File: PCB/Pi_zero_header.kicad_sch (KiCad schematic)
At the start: 44 parts, among them J1 Raspberry_Pi_2_3, J2 USB_C_Receptacle_USB2.0, U1 RP2040, U2 W25Q128JVS, U3 TB6612FNG, U6 PQ25792RQMR, Y1 Crystal

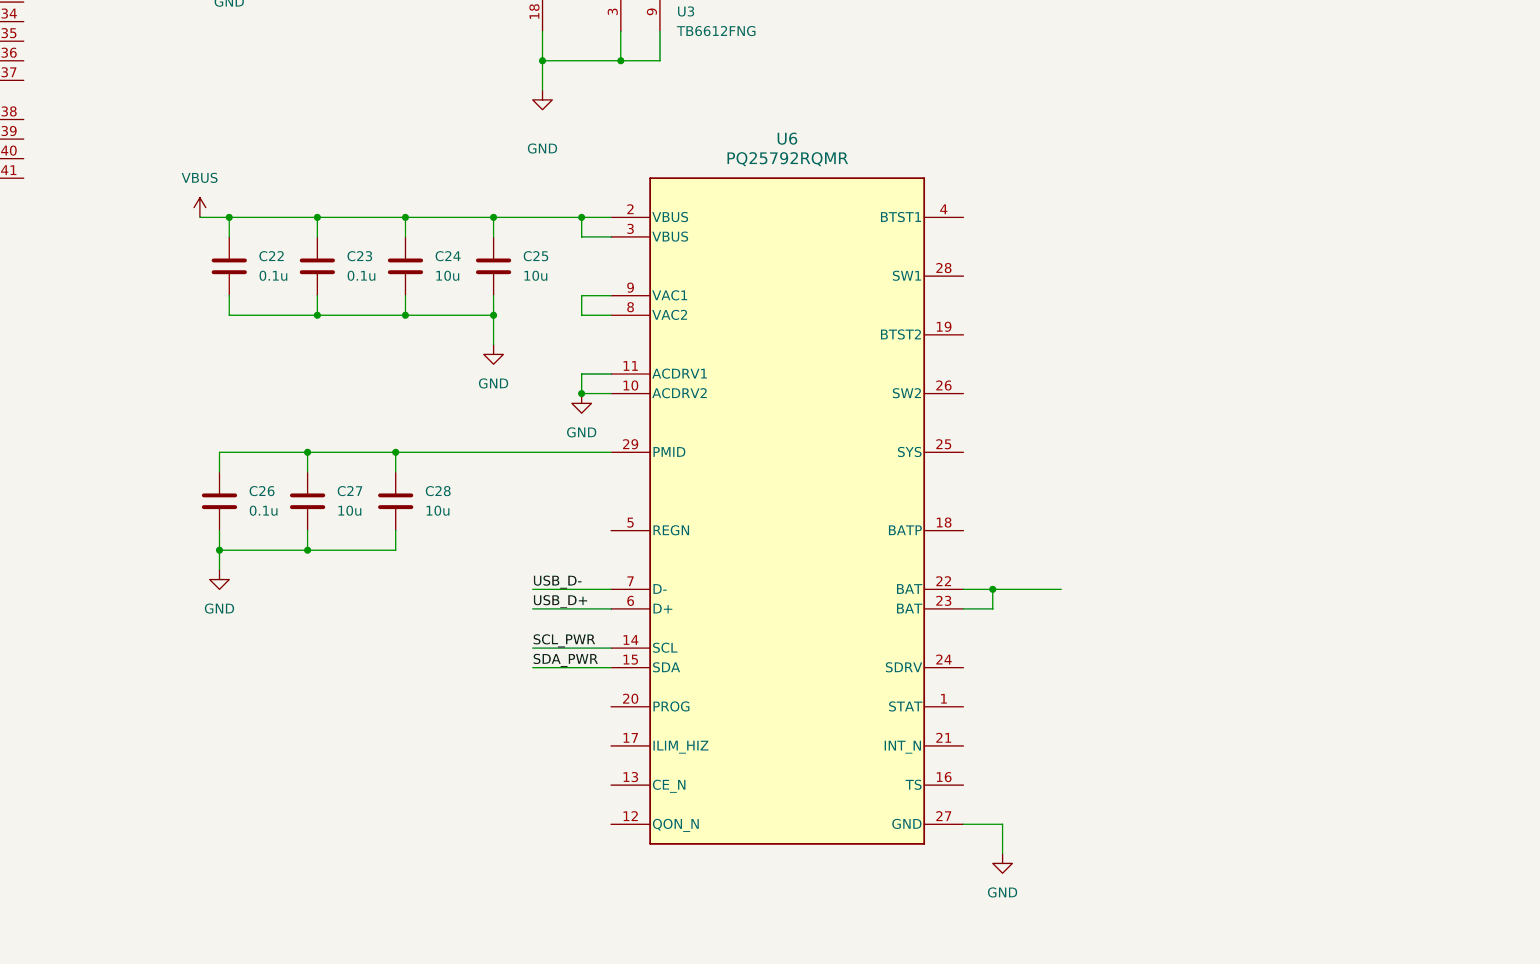
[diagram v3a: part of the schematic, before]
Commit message: Edited schema
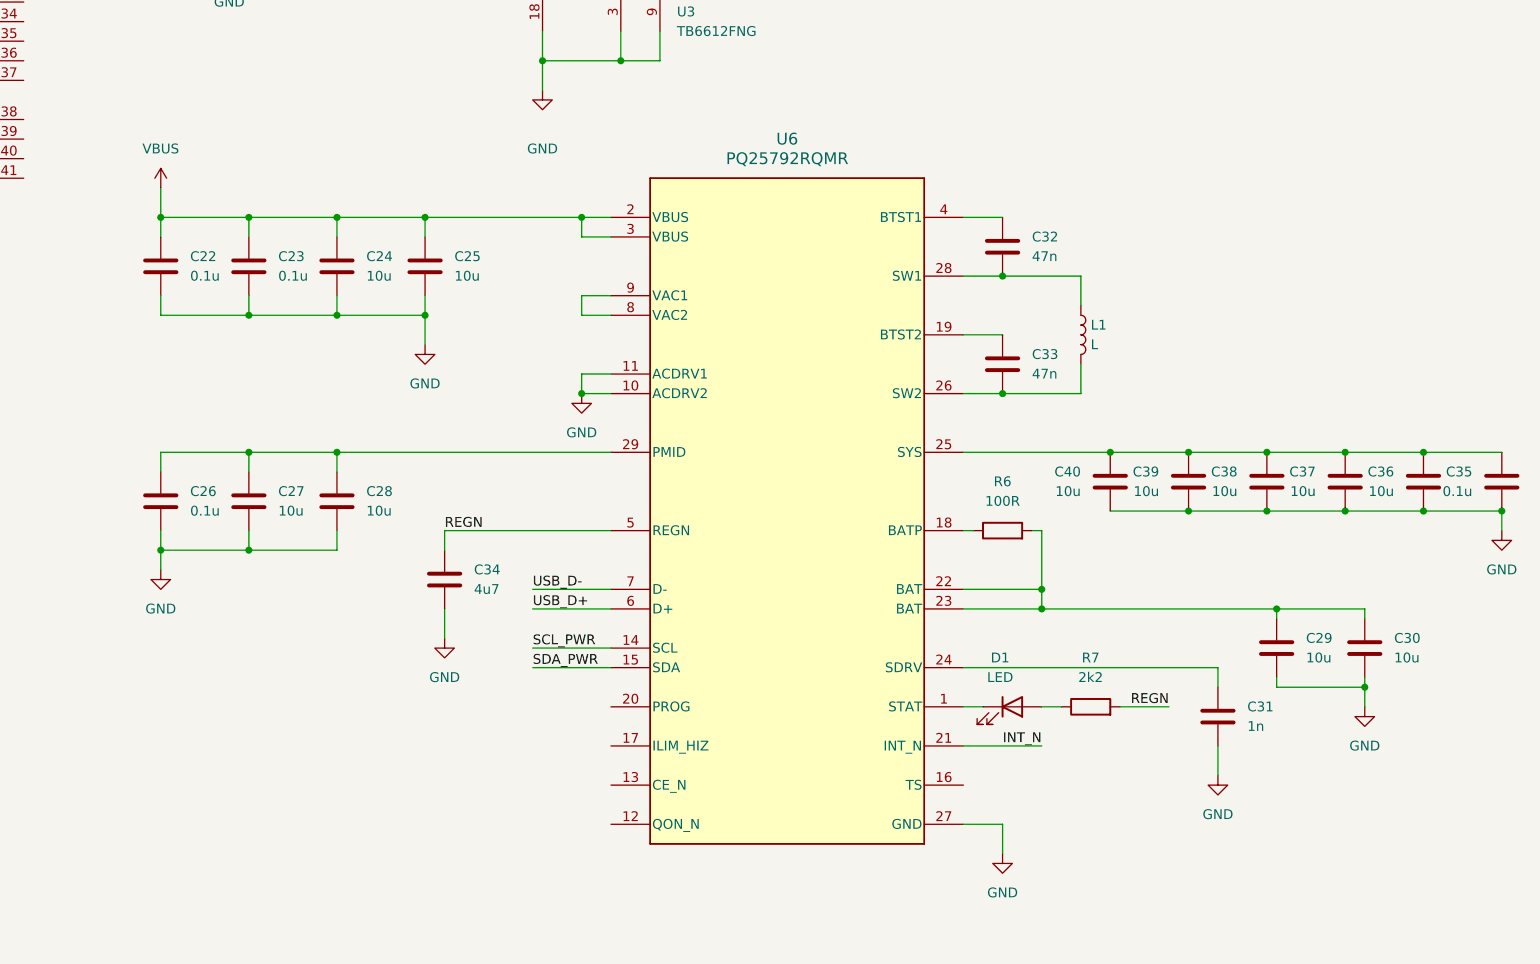
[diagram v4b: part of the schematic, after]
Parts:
- added C29, C30, C36, C37, C38, C39, C40: 10u, symbol Device:C
- added C31: 1n, symbol Device:C
- added C32, C33: 47n, symbol Device:C
- added C34: 4u7, symbol Device:C
- added C35: 0.1u, symbol Device:C
- added D1: LED, symbol Device:LED
- added L1: L, symbol Device:L
- added R6: 100R, symbol Device:R
- added R7: 2k2, symbol Device:R
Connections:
- net GND: now also C29.2, C30.2, C31.2, C34.2, C35.2, C36.2, C37.2, C38.2, C39.2, C40.2
- net at U6.1 (STAT): now also D1.1 (K)
- net at U6.18 (BATP): now also R6.1
- net at U6.19 (BTST2): now also C33.1
- net INT_N: now reaches U6.21 (INT_N)
- net at U6.22 (BAT), U6.23 (BAT): now also C29.1, C30.1, R6.2
- net at U6.24 (SDRV): now also C31.1
- net at U6.25 (SYS): now also C35.1, C36.1, C37.1, C38.1, C39.1, C40.1
- net at U6.26 (SW2): now also C33.2, L1.2
- net at U6.28 (SW1): now also C32.2, L1.1
- net at U6.4 (BTST1): now also C32.1
- net REGN: now reaches U6.5 (REGN)
- net REGN: now also C34.1, R7.2
- new net: D1.2 (A), R7.1
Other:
- moved on the sheet: C22, C23, C24, C25, C26, C27, C28

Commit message: Some changes
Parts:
- removed C1, C4: 10u, symbol Device:C
- added J3, J4: Screw_Terminal_01x02, TerminalBlock_TE-Connectivity:TerminalBlock_TE_282834-2_1x02_P2.54mm_Horizontal, symbol Connector:Screw_Terminal_01x02
- added SW1: SW_Push, Button_Switch_SMD:SW_Push_1P1T_NO_Vertical_Wuerth_434133025816, symbol Switch:SW_Push
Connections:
- net +5V: no longer C18.1, C19.1, U3.13 (VM2), U3.14 (VM3), U3.24 (VM1)
- net GND: now also SW1.1
- net VDD: now reaches C35.1, C36.1, C37.1, C38.1, C39.1, C40.1, U6.25 (SYS)
- net VDD: now also C18.1, C19.1, U3.13 (VM2), U3.14 (VM3), U3.24 (VM1)
- net at R1.1: now also SW1.2
- net at U3.1 (AO1), U3.2 (AO1): now also J3.1 (Pin_1)
- net at U3.11 (BO1), U3.12 (BO1): now also J4.1 (Pin_1)
- net at U3.5 (AO2), U3.6 (AO2): now also J3.2 (Pin_2)
- net at U3.7 (BO2), U3.8 (BO2): now also J4.2 (Pin_2)
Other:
- moved on the sheet: C10, C11, C12, C13, C14, C15, C16, C17, C18, C19, C2, C20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

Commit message: Bruuuh...
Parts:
- added R10: 10k, symbol Device:R
- added R11: 6k04, symbol Device:R
- added R12: 127k, symbol Device:R
- added R13: 100k, symbol Device:R
- added R8: 5k24, symbol Device:R
- added R9: 30k31, symbol Device:R
- C18, C20, C22, C23, C26, C35: value 0.1u -> 100n
- L1: value L -> 1u
- R7: value 2k2 -> 3k3
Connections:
- net GND: now also R10.2, R11.2, R13.2, R9.2
- net REGN: now also R12.2, R8.2
- net USB_D+: no longer U6.6 (D+)
- net USB_D-: no longer U6.7 (D-)
- net at U6.16 (TS): now also R10.1, R8.1, R9.1
- net at U6.17 (ILIM_HIZ): now also R12.1, R13.1
- net at U6.20 (PROG): now also R11.1
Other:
- moved on the sheet: C29, C30, C31, C34, R7

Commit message: Added buck-boost converter to schema
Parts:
- added C1, C4, C41, C43: 10u, symbol Device:C
- added C42: 100n, symbol Device:C
- added C44, C45, C46: 22u, symbol Device:C
- added L2: 1u, symbol Device:L
- added R14: 10k, symbol Device:R
- added R15: 680k, symbol Device:R
- added R16: 100k, symbol Device:R
- added R17: 130k, symbol Device:R
- added U4: TPS630701RNMR, RNM0015A:RNM0015A, symbol TPS63070RNMR:TPS630701RNMR
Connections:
- net +5V: now also C43.1, C44.1, C45.1, C46.1, R15.1, R16.1, U4.7 (VOUT), U4.8 (VOUT)
- net GND: now also C1.2, C4.2, C41.2, C42.2, C43.2, C44.2, C45.2, C46.2, R17.2, U4.10 (PGND), U4.15 (VSEL), U4.4 (GND), U4.6 (FB2)
- new net: C1.1, C4.1, C41.1, R14.1, U4.12 (VIN), U4.13 (VIN)
- new net: R14.2, U4.1 (PS_SYNC), U4.14 (EN)
- new net: C42.1, U4.3 (VAUX)
- new net: R15.2, R17.1, U4.5 (FB)
- new net: L2.1, U4.11 (L1)
- new net: L2.2, U4.9 (L2)
- new net: R16.2, U4.2 (PG)
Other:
- moved on the sheet: C10, C11, C12, C13, C14, C15, C16, C17, C18, C19, C2, C20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

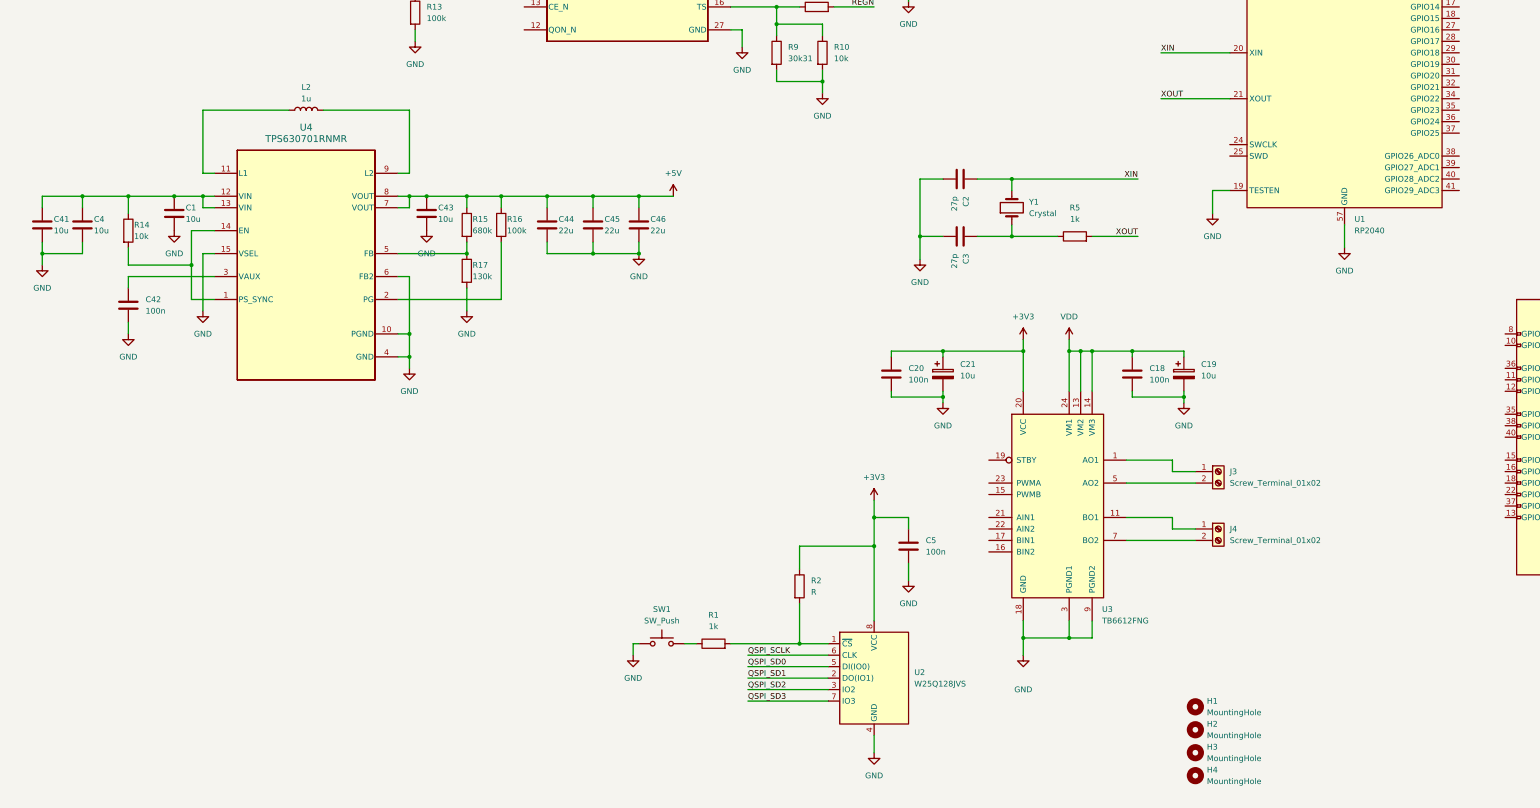
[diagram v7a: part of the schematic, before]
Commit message: Added second buck-boost converter
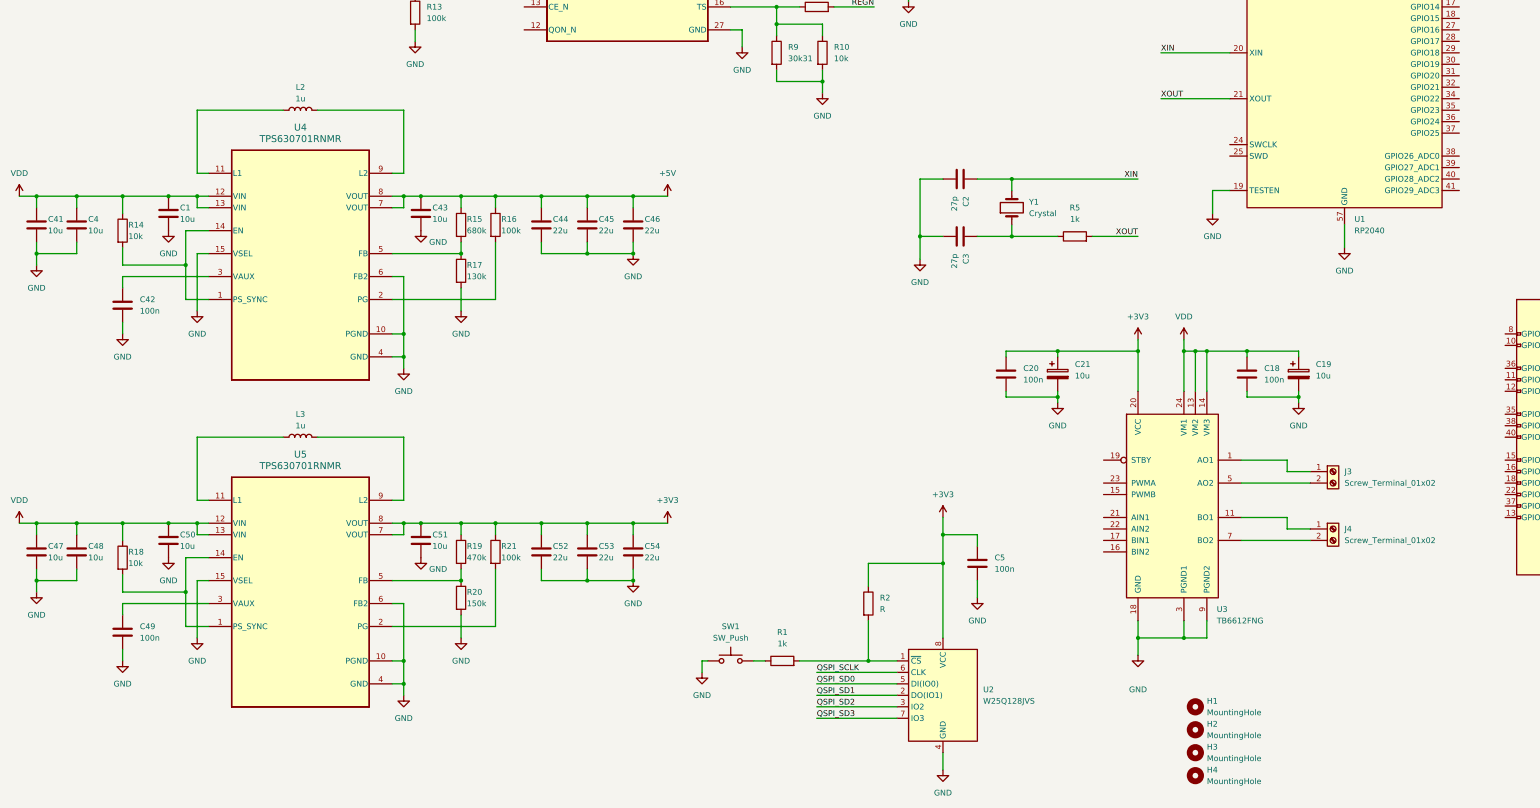
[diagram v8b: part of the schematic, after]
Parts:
- added C47, C48, C50, C51: 10u, symbol Device:C
- added C49: 100n, symbol Device:C
- added C52, C53, C54: 22u, symbol Device:C
- added L3: 1u, symbol Device:L
- added R18: 10k, symbol Device:R
- added R19: 470k, symbol Device:R
- added R20: 150k, symbol Device:R
- added R21: 100k, symbol Device:R
- added U5: TPS630701RNMR, RNM0015A:RNM0015A, symbol TPS63070RNMR:TPS630701RNMR
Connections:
- net +3V3: now also C51.1, C52.1, C53.1, C54.1, R19.1, R21.1, U5.7 (VOUT), U5.8 (VOUT)
- net GND: now also C47.2, C48.2, C49.2, C50.2, C51.2, C52.2, C53.2, C54.2, R20.2, U5.10 (PGND), U5.15 (VSEL), U5.4 (GND), U5.6 (FB2)
- net VDD: now also C1.1, C4.1, C41.1, R14.1, U4.12 (VIN), U4.13 (VIN), C47.1, C48.1, C50.1, R18.1, U5.12 (VIN), U5.13 (VIN)
- new net: C49.1, U5.3 (VAUX)
- new net: R21.2, U5.2 (PG)
- new net: R18.2, U5.1 (PS_SYNC), U5.14 (EN)
- new net: R19.2, R20.1, U5.5 (FB)
- new net: L3.1, U5.11 (L1)
- new net: L3.2, U5.9 (L2)
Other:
- moved on the sheet: C1, C18, C19, C20, C21, C4, C41, C42, C43, C44, C45, C46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
